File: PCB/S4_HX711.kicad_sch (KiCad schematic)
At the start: 12 parts, among them J3 LOADCELL, Q1 Q_PNP_BEC, U2 HX711

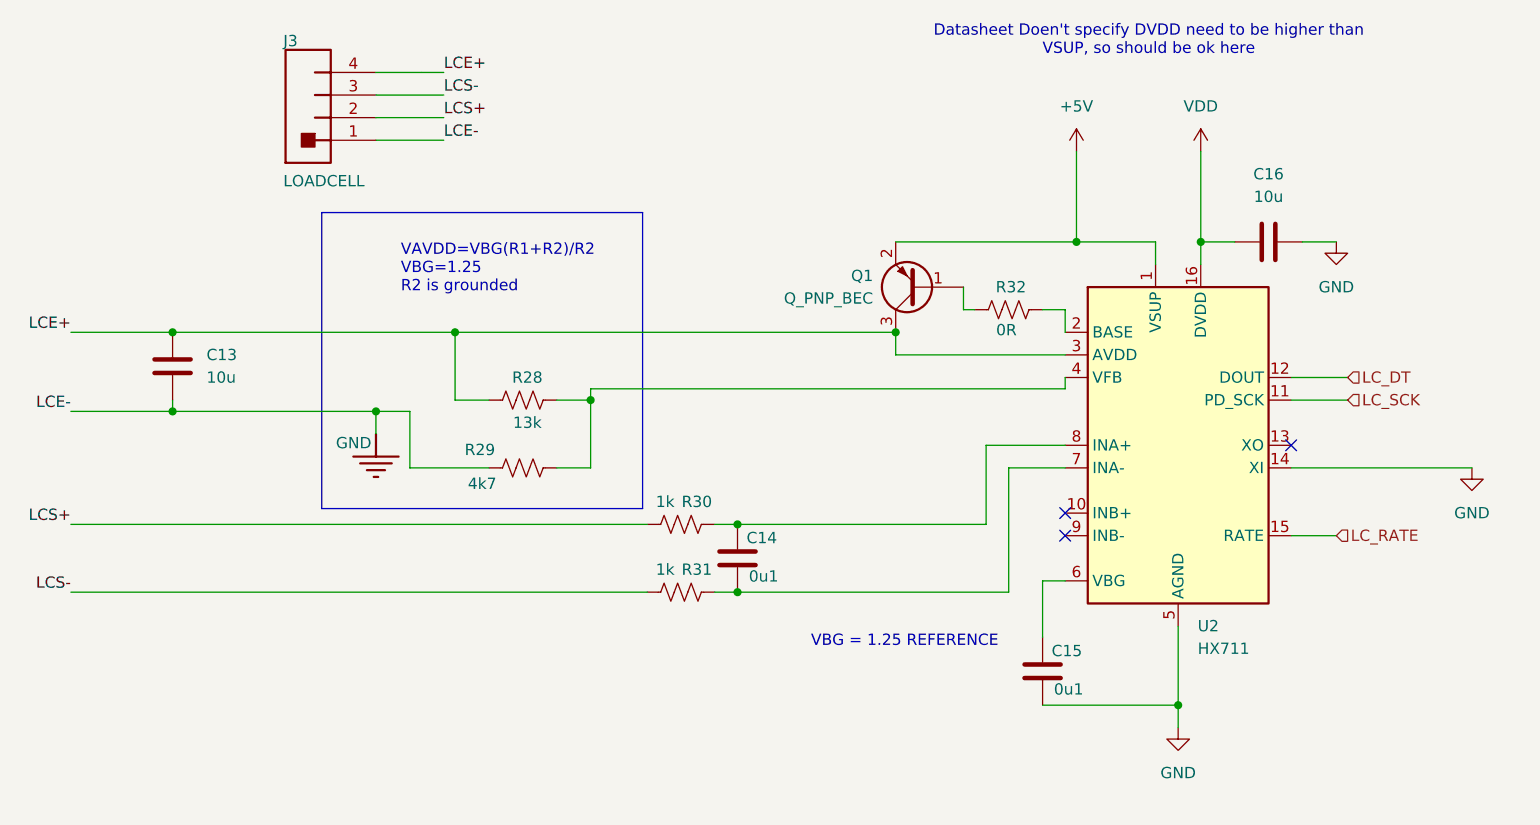
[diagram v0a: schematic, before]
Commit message: Update PCB to seperate ground symbols apporiately. Modify board to sepearte ground path for motor current and all other devices. Add filtering for slide power, hopefully reduce bownout or other issue.
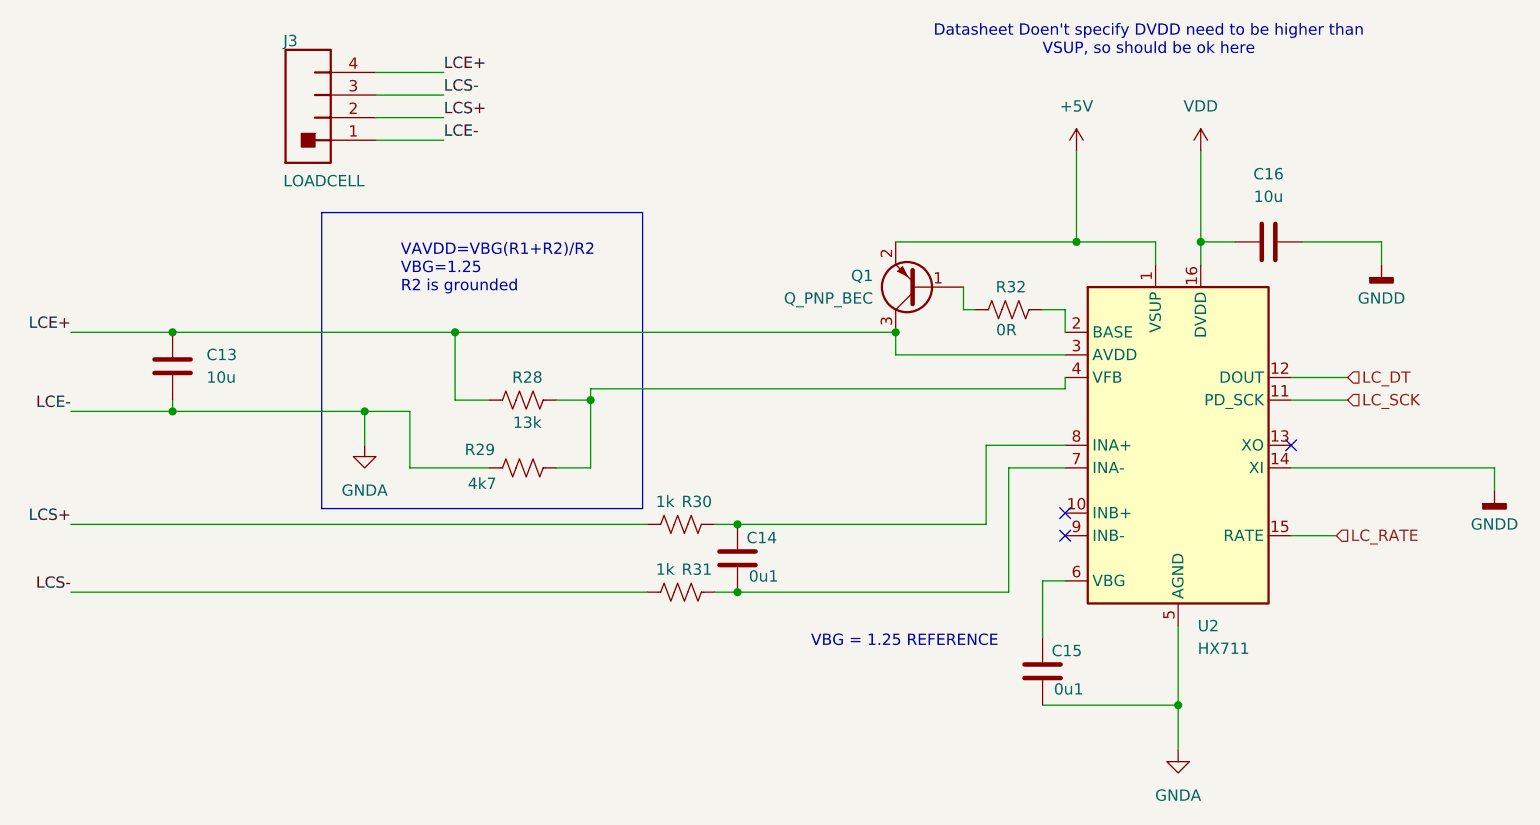
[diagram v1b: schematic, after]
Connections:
- net GND renamed GNDA
- net GNDA: no longer C16.2, U2.14 (XI)
- new net GNDD: C16.2, U2.14 (XI)
